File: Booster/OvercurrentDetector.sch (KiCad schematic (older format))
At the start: 35 parts, among them U203 LM339, U501 LM338, U502 LM358, U503 NE555

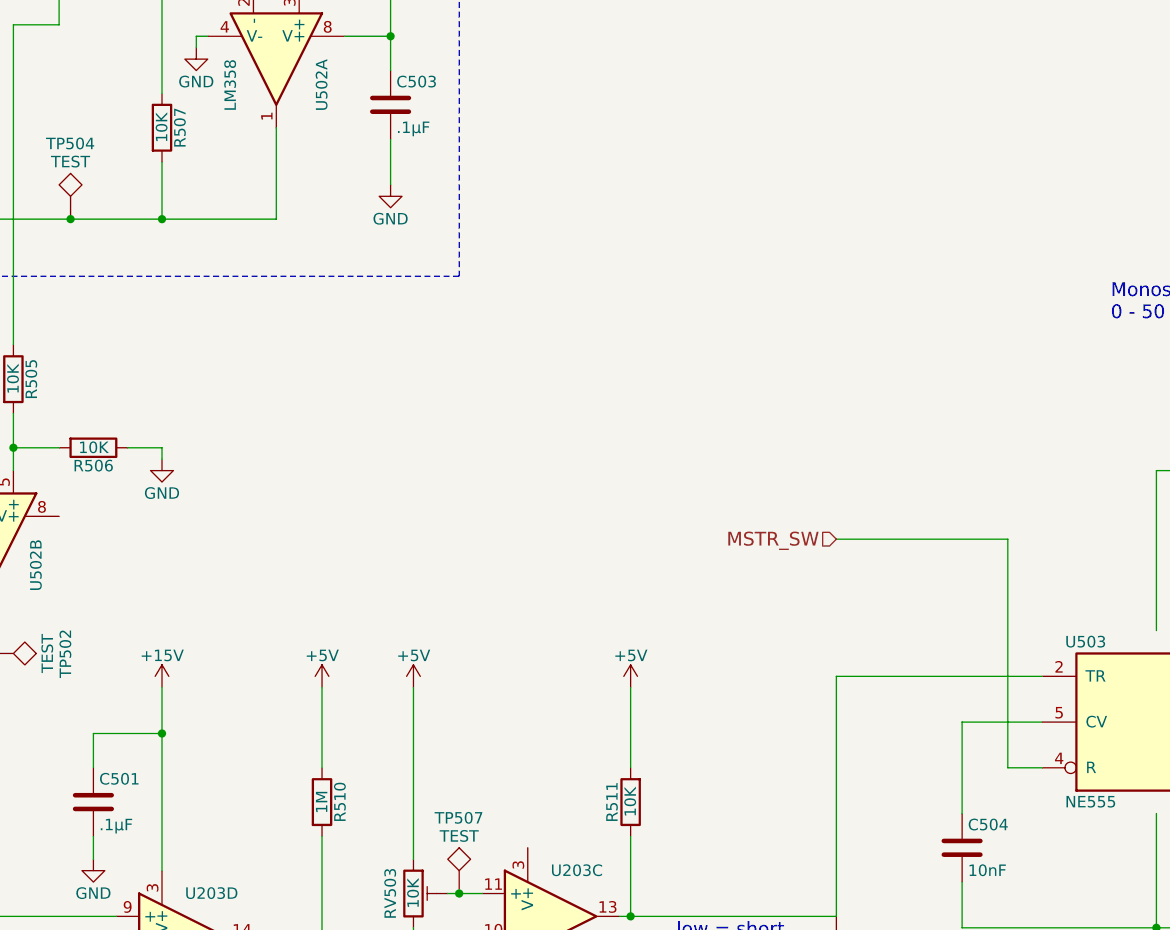
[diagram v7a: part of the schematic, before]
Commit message: Replaced NAND gate with AND as the additional NOT gates ended up only used to negate the NAND gates directly. One extra AND gate used to allow resetting overcurrent by either master switch or DCC disable/enable.
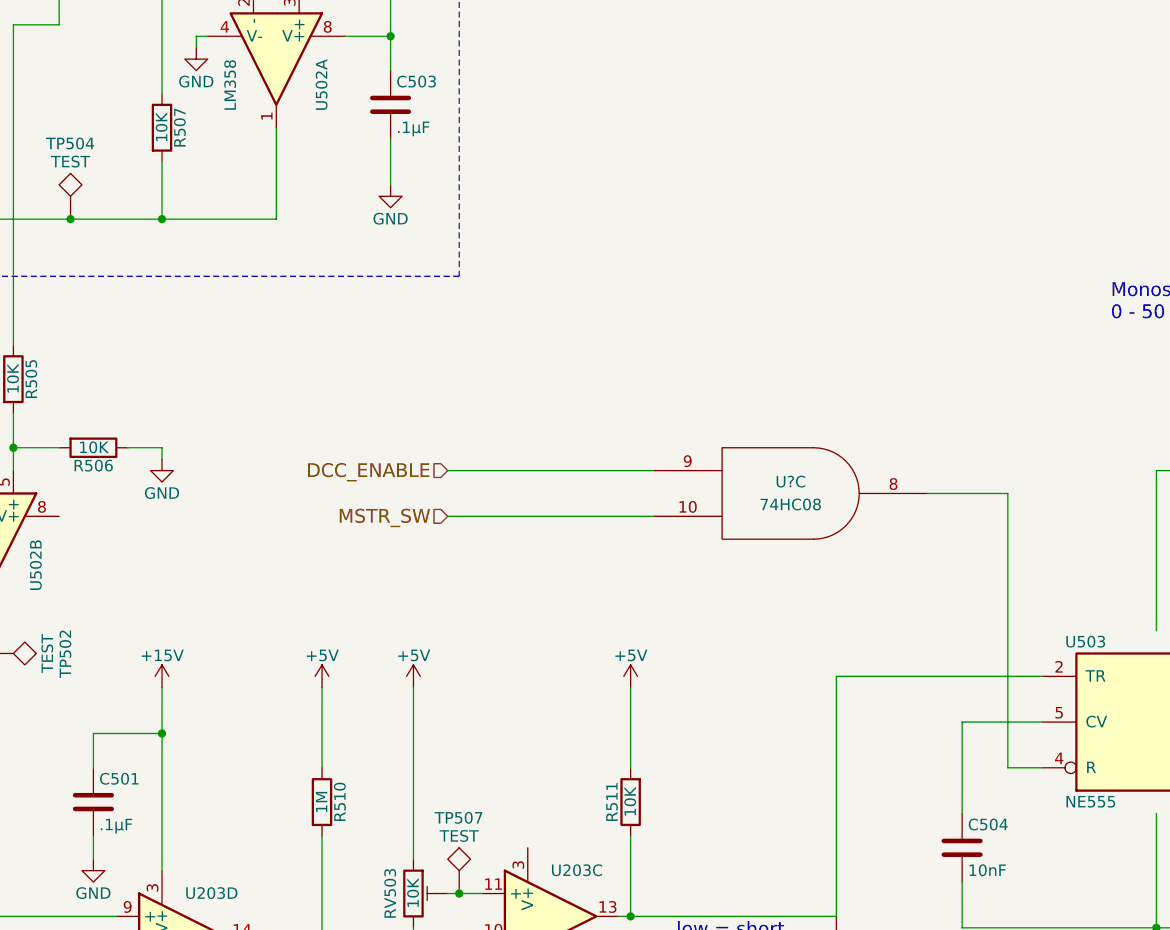
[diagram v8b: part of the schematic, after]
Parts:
- added U?: 74HC08, symbol 74LS08
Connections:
- net +5V: now also U?.14 (VCC)
- net GND: now also U?.7 (GND)
- net MSTR_SW: now also U?.10; no longer U503.4 (R)
- new net: U503.4 (R), U?.8
- new net DCC_ENABLE: U?.9
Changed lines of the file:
@@
 	4400 2900 4400 2500
 Wire Wire Line
-	3900 2650 3900 2900
+	3900 2900 3900 2650
 Connection ~ 3900 2900
 Wire Wire Line
@@
 	7600 5300 7750 5300
 Wire Wire Line
-	7600 4300 7600 5300
+	7600 4100 7600 5300
 Wire Wire Line
 	8750 5100 9000 5100
@@
 	0    1    1    0
 $EndComp
-Text HLabel 6850 4300 0    60   Input ~ 0
+Text HLabel 5150 4200 0    60   Input ~ 0
 MSTR_SW
-Wire Wire Line
-	7600 4300 6850 4300
 Wire Wire Line
 	4500 1000 4500 1900
@@
 	5150 5850 5300 5850
 Connection ~ 5200 5850
+$Comp
+L 74LS08 U?
+U 3 1 5A3EBEE8
+P 6650 4100
+F 0 "U?" H 6650 4150 50  0000 C CNN
+F 1 "74HC08" H 6650 4050 50  0000 C CNN
+F 2 "" H 6650 4100 50  0000 C CNN
+F 3 "" H 6650 4100 50  0000 C CNN
+	3    6650 4100
+	1    0    0    -1
+$EndComp
+Wire Wire Line
+	7250 4100 7600 4100
+Wire Wire Line
+	5150 4200 6050 4200
+Text HLabel 5150 4000 0    60   Input ~ 0
+DCC_ENABLE
+Wire Wire Line
+	5150 4000 6050 4000
 $EndSCHEMATC
